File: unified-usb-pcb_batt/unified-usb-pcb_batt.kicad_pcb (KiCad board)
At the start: 2 copper layers, 30 x 34 mm, 39 parts, among them J1 QI, J2 USB_C_Receptacle_USB2.0, J3 USB_Out, J4 BATT, J5 THERM, SW1 SW_SPDT, U1 SRV05-4, U2 DW01A, U3 TP4056, U4 FS8205

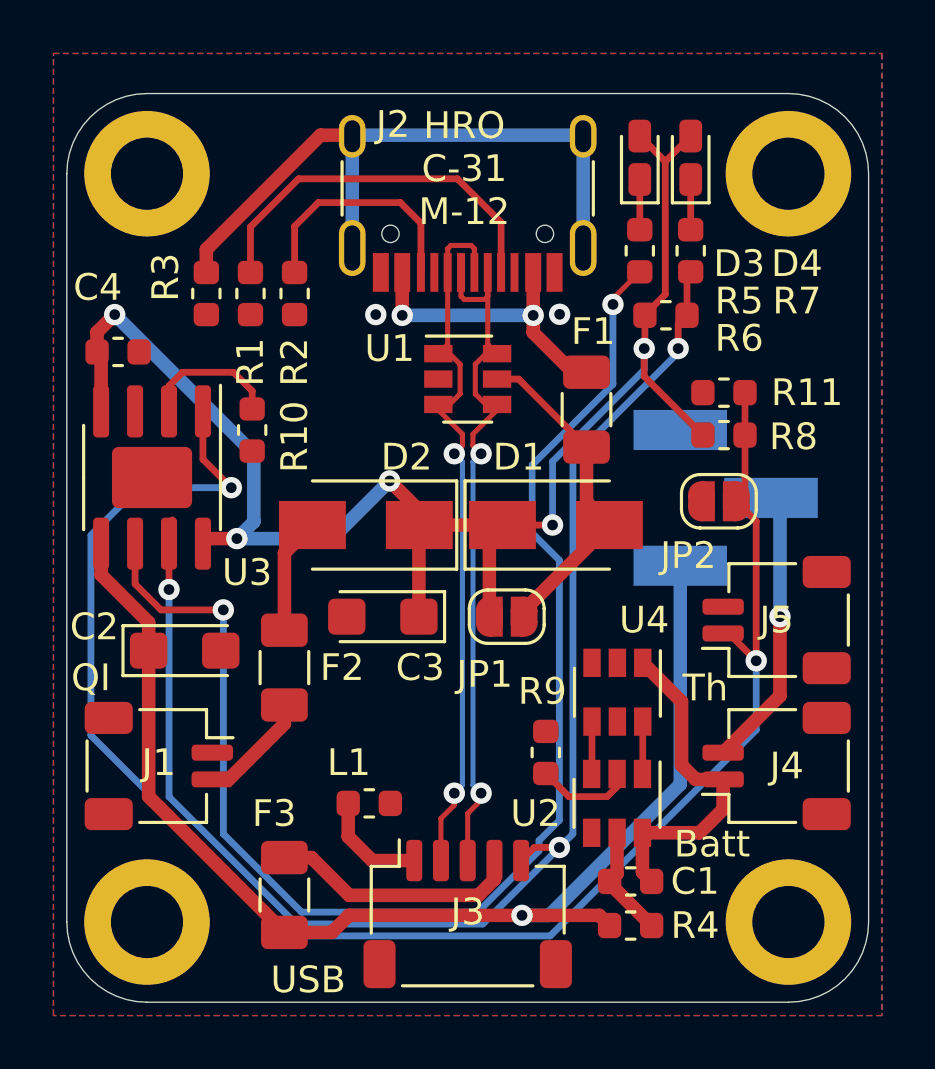
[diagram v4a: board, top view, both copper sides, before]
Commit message: moved traces for better ground pour, added a probably unneccessary amount of vias
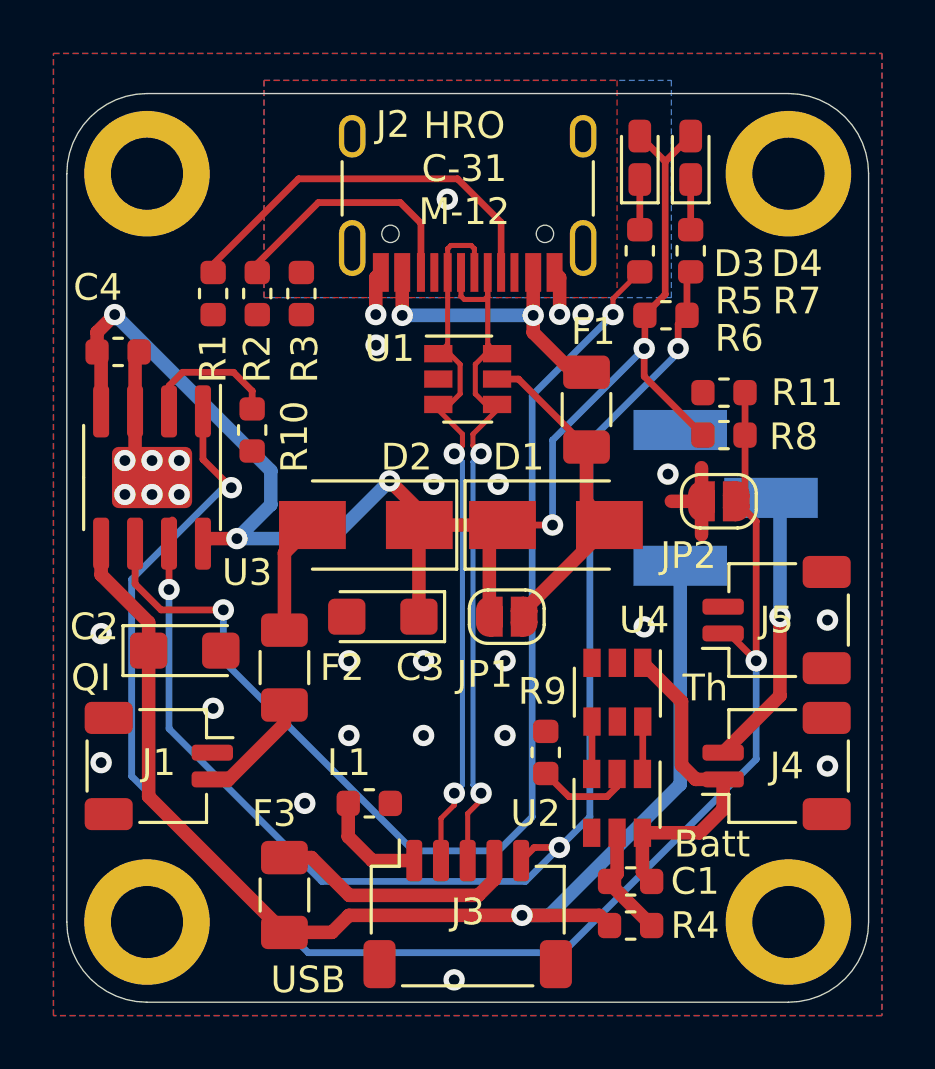
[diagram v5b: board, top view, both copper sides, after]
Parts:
- moved R3 3.56 mm to (24.5, 26.8)
- moved R1 1.40 mm to (21.2, 26.8)
- moved R2 1.40 mm to (22.9, 26.8)
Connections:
- U3 pad 9: (no net) -> GNDPWR
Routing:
- net Net-(J2-PadS1): track 25.1 -> 0.00 mm, vias 0 -> 1
- net GNDPWR: track 0.57 -> 12.5 mm, vias 2 -> 27
- net Net-(R5-Pad1): track 52.7 -> 45.3 mm
- net chgsense: track 52.5 -> 49.7 mm
- net Net-(J5-Pad1): track 62.7 -> 60.7 mm
- net Net-(J2-PadB5): track 8.94 -> 9.52 mm
- net Net-(J2-PadA5): track 14.3 -> 14.9 mm
- net +5V: track 59.1 -> 59.6 mm
- added copper zone on B.Cu, net Net-(J2-PadS1)
- added copper zone on F.Cu, net Net-(J2-PadS1)

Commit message: changed jumper pad, fixed silk
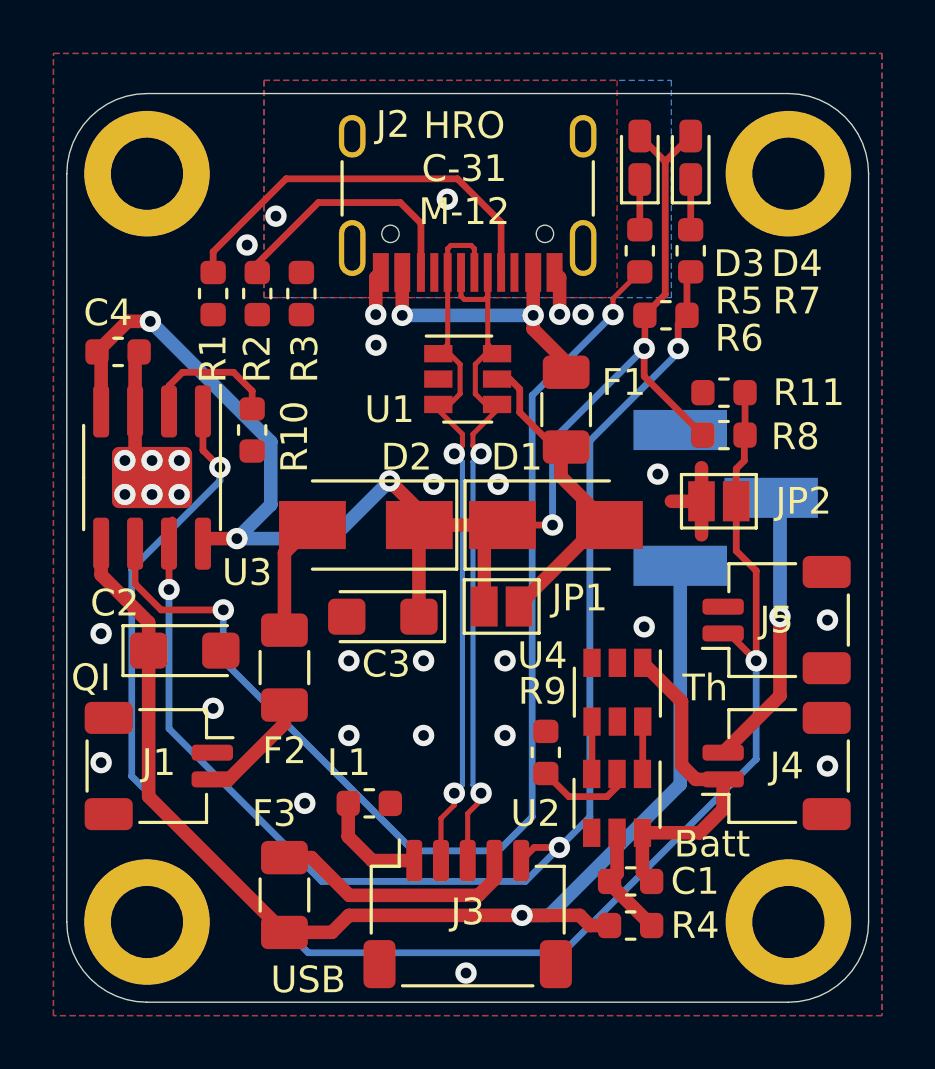
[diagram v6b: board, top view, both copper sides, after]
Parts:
- F1, F2, F3: value 1206L050/15YR -> SCF075-1206R
- JP1, JP2: footprint Jumper:SolderJumper-2_P1.3mm_Open_RoundedPad1.0x1.5mm -> Jumper:SolderJumper-2_P1.3mm_Open_Pad1.0x1.5mm
- L1: value BLM18PG121SN1D -> PBY160808T-181Y-N
- moved F1 0.76 mm to (34.4, 31.1)
- moved JP1 0.43 mm to (32.0, 38.5)
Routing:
- net Net-(F1-Pad2): track 11.4 -> 10.8 mm
- net Net-(J5-Pad1): track 60.7 -> 60.2 mm
- net Net-(J2-PadS1): vias 1 -> 2
- net GNDPWR: vias 27 -> 28
